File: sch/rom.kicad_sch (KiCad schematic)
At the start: 10 parts

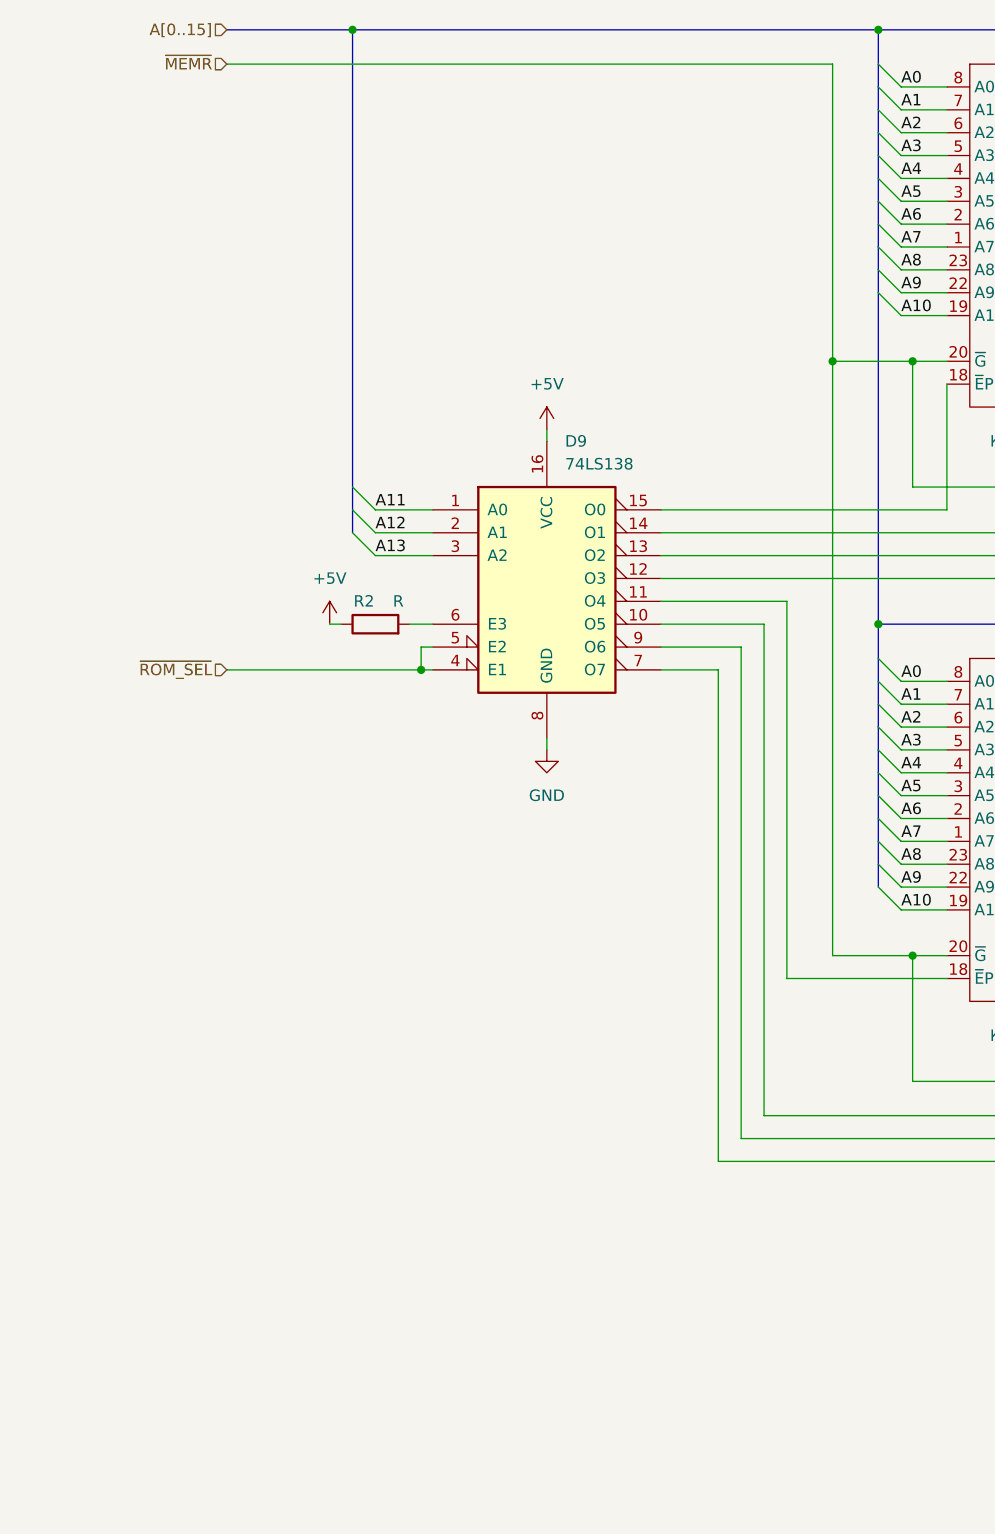
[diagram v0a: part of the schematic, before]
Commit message: Sch: mem remapping circuit moved to ROM sheet
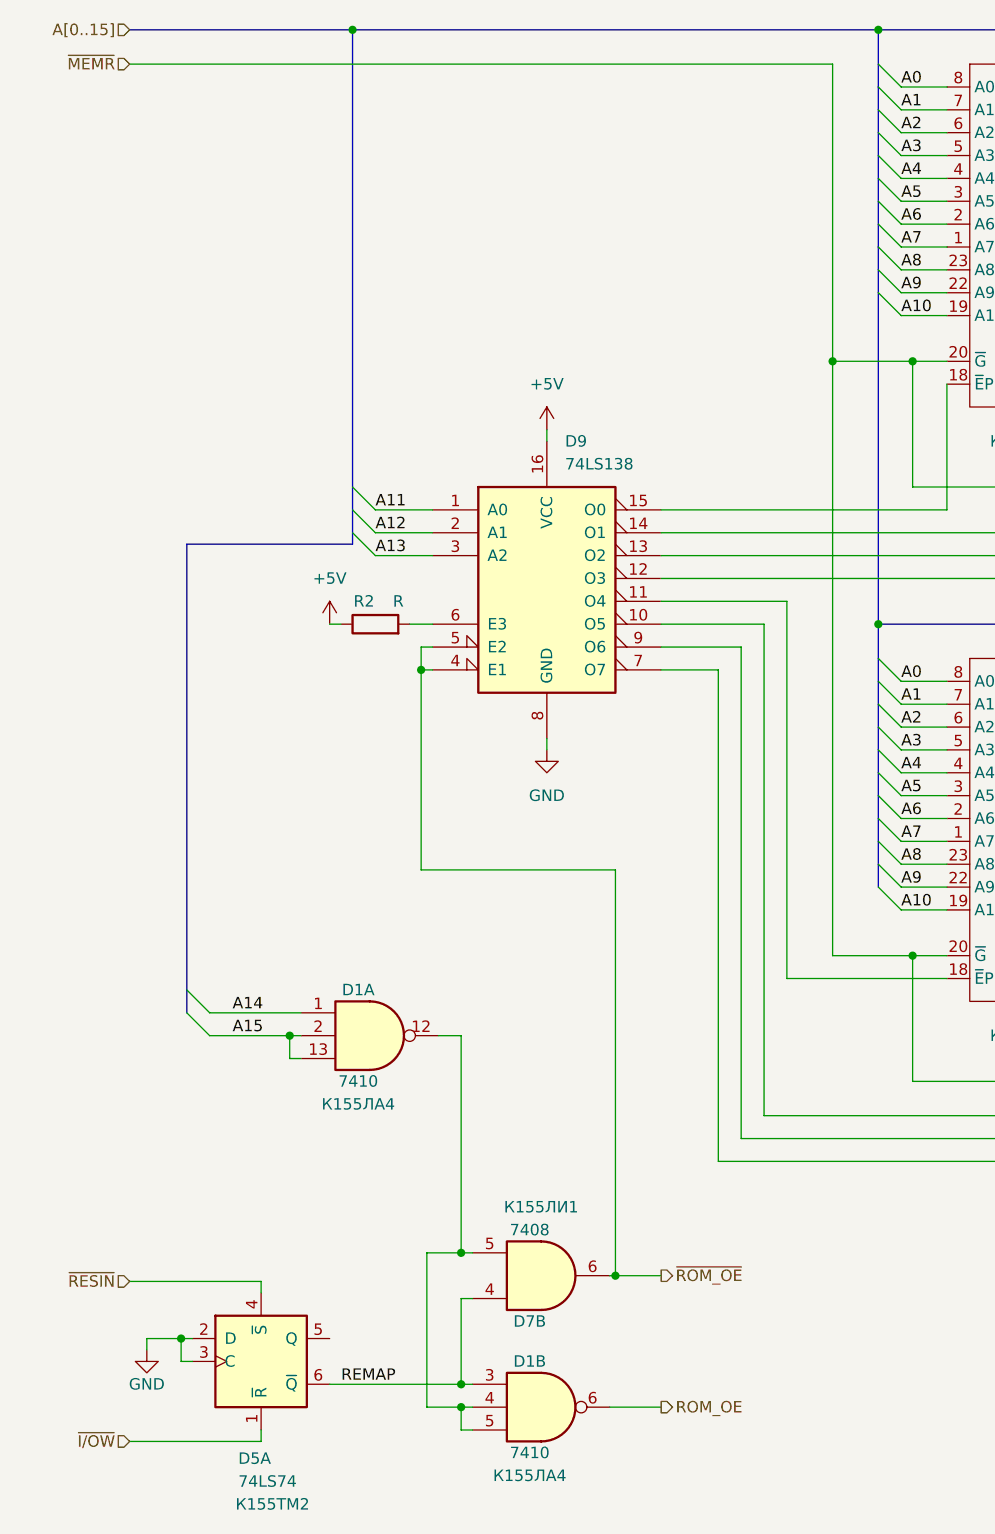
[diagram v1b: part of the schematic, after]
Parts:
- added D1: 7410, symbol 74xx:74LS10
- added D5: 74LS74, symbol 74xx:74LS74
- added D7: 7408, symbol 74xx:74LS08
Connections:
- net GND: now also D5.2 (D), D5.3 (C)
- net ~{ROM_SEL} renamed ~{ROM_OE}
- net ~{ROM_OE}: now also D7.6
- new net: D1.12, D1.4, D1.5, D7.5
- new net A14: D1.1
- new net A15: D1.13, D1.2
- new net REMAP: D1.3, D5.6 (~{Q}), D7.4
- new net ROM_OE: D1.6
- new net ~{I/OW}: D5.1 (~{R})
- new net ~{RESIN}: D5.4 (~{S})

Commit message: Schematics complete
Todo:
- part values
- full review
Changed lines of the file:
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@@
     (effects (font (size 1.27 1.27)) (justify right))
   )
-  (hierarchical_label "D[0..7]" (shape input) (at 269.24 134.62 0)
+  (hierarchical_label "D[0..7]" (shape output) (at 269.24 134.62 0)
     (effects (font (size 1.27 1.27)) (justify left))
   )

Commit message: Schematics completed with values
Visual corrections pending
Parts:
- D11, D12, D13: value ~ -> 2716
- D5: value 74LS74 -> 7474
- D9: CCCP (none) -> К555ИД7
- R2: value R -> 1k
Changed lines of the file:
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@@
     (in_bom yes) (on_board yes)
     (property "Reference" "D12" (id 0) (at 209.55 22.86 0))
-    (property "Value" "~" (id 1) (at 209.55 63.5 0))
+    (property "Value" "2716" (id 1) (at 209.55 63.5 0))
     (property "Footprint" "" (id 2) (at 203.2 24.13 0)
       (effects (font (size 1.27 1.27)) hide)
@@
       (effects (font (size 1.27 1.27)) (justify left))
     )
-    (property "Value" "74LS74" (id 1) (at 45.72 181.61 0)
+    (property "Value" "7474" (id 1) (at 45.72 181.61 0)
       (effects (font (size 1.27 1.27)) (justify left))
     )
@@
     (in_bom yes) (on_board yes)
     (property "Reference" "R2" (id 0) (at 59.69 83.82 90))
-    (property "Value" "R" (id 1) (at 63.5 83.82 90))
+    (property "Value" "1k" (id 1) (at 63.5 83.82 90))
     (property "Footprint" "" (id 2) (at 60.96 88.138 90)
       (effects (font (size 1.27 1.27)) hide)
@@
     )
     (property "Datasheet" "http://www.ti.com/lit/gpn/sn74LS138" (id 3) (at 80.01 81.28 0)
+      (effects (font (size 1.27 1.27)) hide)
+    )
+    (property "CCCP" "К555ИД7" (id 4) (at 80.01 81.28 0)
       (effects (font (size 1.27 1.27)) hide)
     )
@@
     (in_bom yes) (on_board yes)
     (property "Reference" "D13" (id 0) (at 247.65 22.86 0))
-    (property "Value" "~" (id 1) (at 247.65 63.5 0))
+    (property "Value" "2716" (id 1) (at 247.65 63.5 0))
     (property "Footprint" "" (id 2) (at 241.3 24.13 0)
       (effects (font (size 1.27 1.27)) hide)
@@
     (in_bom yes) (on_board yes)
     (property "Reference" "D11" (id 0) (at 171.45 22.86 0))
-    (property "Value" "~" (id 1) (at 171.45 63.5 0))
+    (property "Value" "2716" (id 1) (at 171.45 63.5 0))
     (property "Footprint" "" (id 2) (at 165.1 24.13 0)
       (effects (font (size 1.27 1.27)) hide)

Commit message: Sch: visual corrections
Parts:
- D1: value 7410 -> 74LS10
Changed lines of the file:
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@@
     (in_bom yes) (on_board yes)
     (property "Reference" "D1" (id 0) (at 78.105 168.275 0))
-    (property "Value" "7410" (id 1) (at 78.105 178.435 0))
+    (property "Value" "74LS10" (id 1) (at 78.105 178.435 0))
     (property "Footprint" "" (id 2) (at 79.375 173.355 0)
       (effects (font (size 1.27 1.27)) hide)
@@
   )
   (symbol (lib_id "74xx:74LS138") (at 80.01 81.28 0) (unit 1)
-    (in_bom yes) (on_board yes) (fields_autoplaced)
+    (in_bom yes) (on_board yes)
     (property "Reference" "D9" (id 0) (at 82.0294 66.04 0)
       (effects (font (size 1.27 1.27)) (justify left))
@@
       (effects (font (size 1.27 1.27)) hide)
     )
-    (property "CCCP" "К555ИД7" (id 4) (at 80.01 81.28 0)
-      (effects (font (size 1.27 1.27)) hide)
-    )
+    (property "CCCP" "К555ИД7" (id 4) (at 87.63 96.52 0))
     (pin "1")
     (pin "10")
@@
     (in_bom yes) (on_board yes)
     (property "Reference" "D1" (id 0) (at 59.055 127 0))
-    (property "Value" "7410" (id 1) (at 59.055 137.16 0))
+    (property "Value" "74LS10" (id 1) (at 59.055 137.16 0))
     (property "Footprint" "" (id 2) (at 60.325 132.08 0)
       (effects (font (size 1.27 1.27)) hide)
